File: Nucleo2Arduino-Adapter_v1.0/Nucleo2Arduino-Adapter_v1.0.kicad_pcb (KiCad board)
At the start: 2 copper layers, 68.6 x 53.3 mm, 12 parts, among them J1 TI_BOOSTER_40_J1, J2 TI_BOOSTER_40_J2, J3 TI_BOOSTER_40_J3, J4 TI_BOOSTER_40_J4, P1 Power, P2 Analog, P3 Digital, P4 Digital, P5 CONN_1, P6 CONN_1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

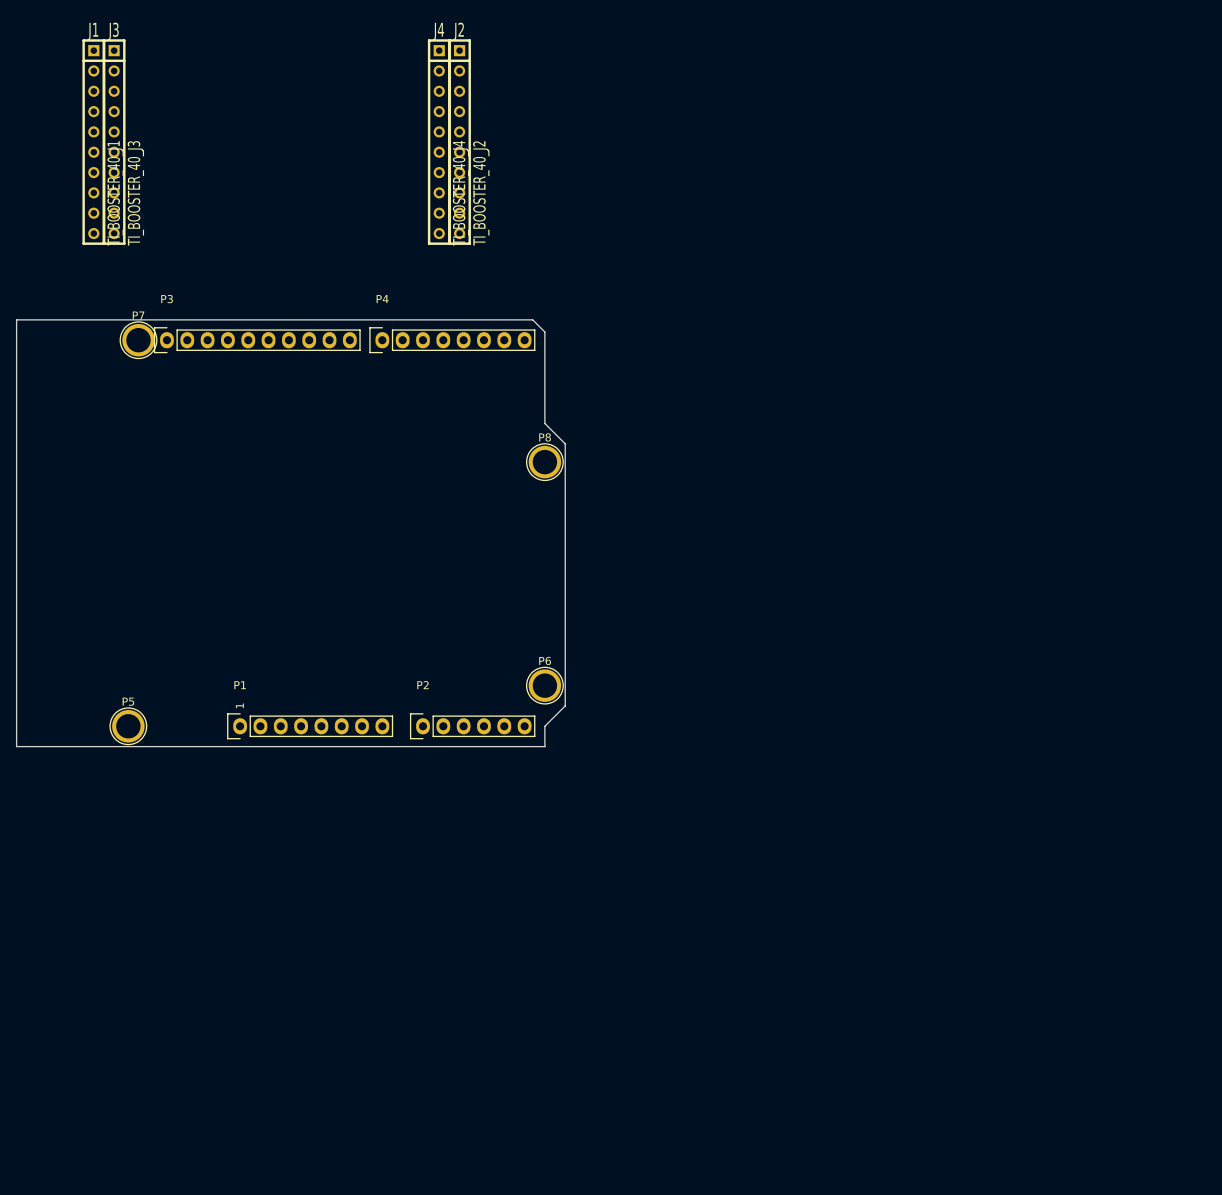
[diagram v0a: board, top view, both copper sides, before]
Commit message: Added ICSP header, Fixed Ardino/BSTPCK Symbols, Added connection
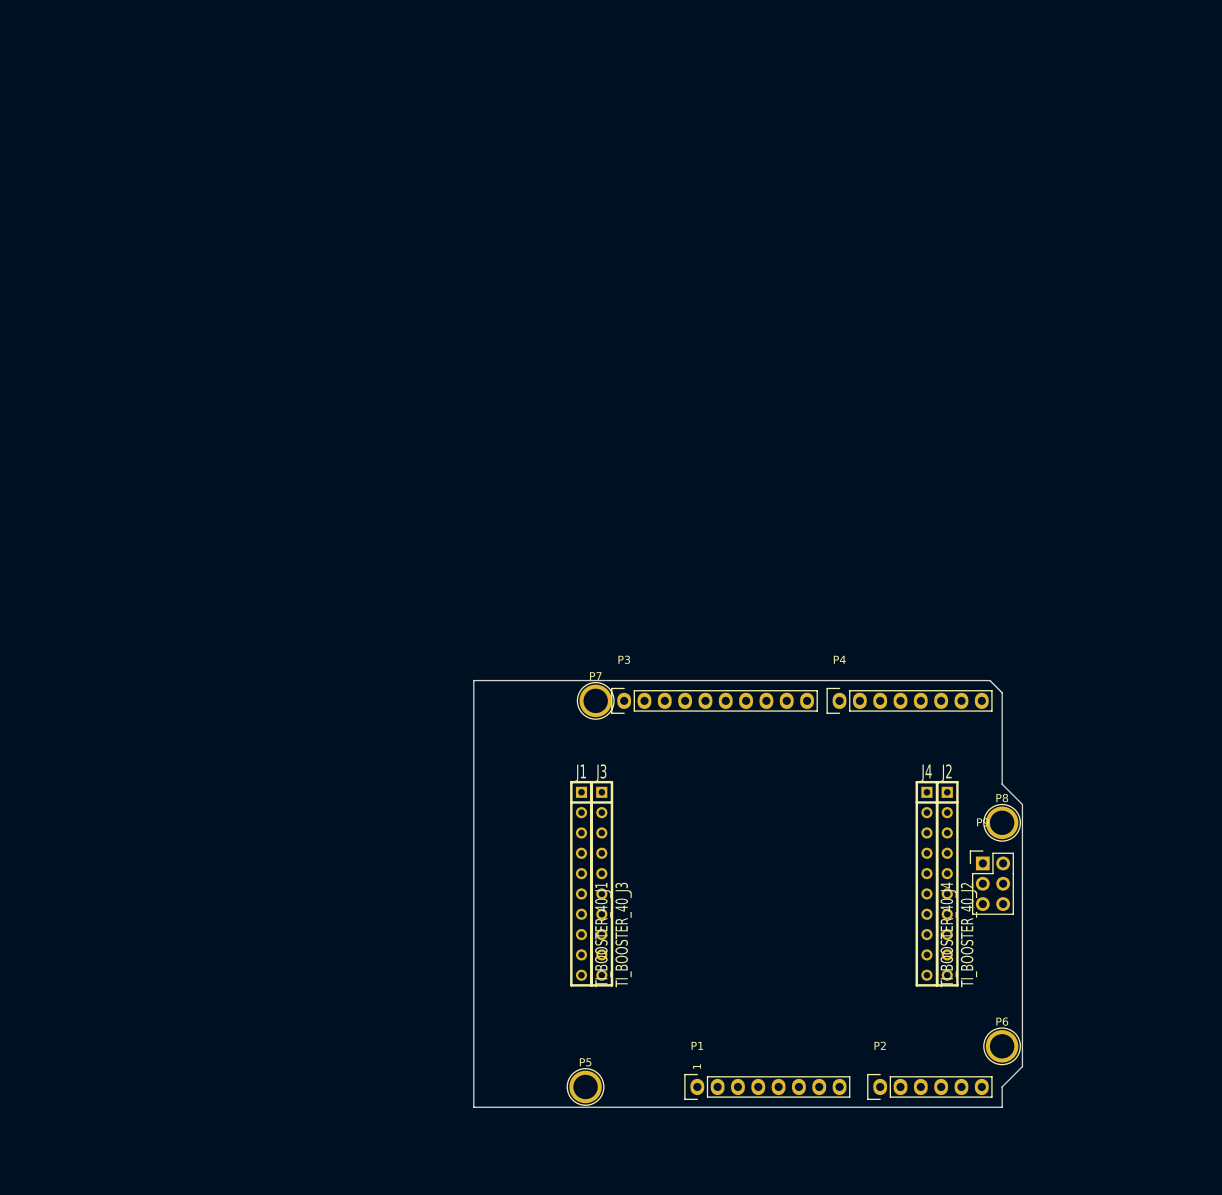
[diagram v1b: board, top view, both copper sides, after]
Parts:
- added P9: ARDUINO_ICSP, Pin_Headers:Pin_Header_Straight_2x03, F.Cu at (244.5, 147.3)
- moved J1 111.0 mm to (194.3, 149.9)
- moved J2 111.0 mm to (240.0, 149.9)
- moved J3 111.0 mm to (196.8, 149.9)
- moved J4 111.0 mm to (237.5, 149.9)
- moved P3 72.8 mm to (199.6, 127.0)
- moved P4 72.8 mm to (226.6, 127.0)
- moved P6 72.8 mm to (246.9, 170.2)
- moved P7 72.8 mm to (196.1, 127.0)
- moved P8 72.8 mm to (246.9, 142.2)
- moved P1 72.8 mm to (208.8, 175.3)
- moved P2 72.8 mm to (231.6, 175.3)
- moved P5 72.8 mm to (194.8, 175.3)
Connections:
- net /10(**/SS) renamed /SPI_0_SS
- net /2 renamed Net-(P4-Pad6)
- net /4 renamed Net-(P4-Pad4)
- net /7 renamed Net-(P4-Pad1)
- net /8 renamed Net-(P3-Pad10)
- net /AREF renamed Net-(P3-Pad3)
- net /IOREF renamed Net-(P1-Pad2)
- net /Vin renamed VDD
- J1 pad 1: VCC -> +3V3
- J1 pad 10: Net-(J1-Pad10) -> /I2C_0_SDA
- J1 pad 2: Net-(J1-Pad2) -> /AIn_0_0
- J1 pad 3: Net-(J1-Pad3) -> /UART_0_RX
- J1 pad 4: Net-(J1-Pad4) -> /UART_0_TX
- J1 pad 6: Net-(J1-Pad6) -> /AIn_0_1
- J1 pad 7: Net-(J1-Pad7) -> /SPI_0_SCK
- J1 pad 9: Net-(J1-Pad9) -> /I2C_0_SCL
- J2 pad 2: Net-(J2-Pad2) -> /PWM_0_1
- J2 pad 5: Net-(J2-Pad5) -> /RESET
- J2 pad 6: Net-(J2-Pad6) -> /SPI_0_MOSI
- J2 pad 7: Net-(J2-Pad7) -> /SPI_0_MISO
- J3 pad 3: Net-(J3-Pad3) -> /AIn_0_2
- J3 pad 4: Net-(J3-Pad4) -> /AIn_0_3
- J3 pad 5: Net-(J3-Pad5) -> /AIn_0_4
- J3 pad 6: Net-(J3-Pad6) -> /AIn_0_5
- J4 pad 1: Net-(J4-Pad1) -> /PWM_0_2
- J4 pad 2: Net-(J4-Pad2) -> /PWM_0_3
- J4 pad 3: Net-(J4-Pad3) -> /PWM_0_4
- P1 pad 3: /Reset -> /RESET
- P2 pad 1: /A0 -> /AIn_0_0
- P2 pad 2: /A1 -> /AIn_0_1
- P2 pad 3: /A2 -> /AIn_0_2
- P2 pad 4: /A3 -> /AIn_0_3
- P2 pad 5: /A4(SDA) -> /AIn_0_4
- P2 pad 6: /A5(SCL) -> /AIn_0_5
- P3 pad 1: /A5(SCL) -> /I2C_0_SCL
- P3 pad 2: /A4(SDA) -> /I2C_0_SDA
- P3 pad 5: /13(SCK) -> /SPI_0_SCK
- P3 pad 6: /12(MISO) -> /SPI_0_MISO
- P3 pad 7: /11(**/MOSI) -> /SPI_0_MOSI
- P3 pad 9: /9(**) -> /PWM_0_1
- P4 pad 2: /6(**) -> /PWM_0_2
- P4 pad 3: /5(**) -> /PWM_0_3
- P4 pad 5: /3(**) -> /PWM_0_4
- P4 pad 7: /1(Tx) -> /UART_0_TX
- P4 pad 8: /0(Rx) -> /UART_0_RX

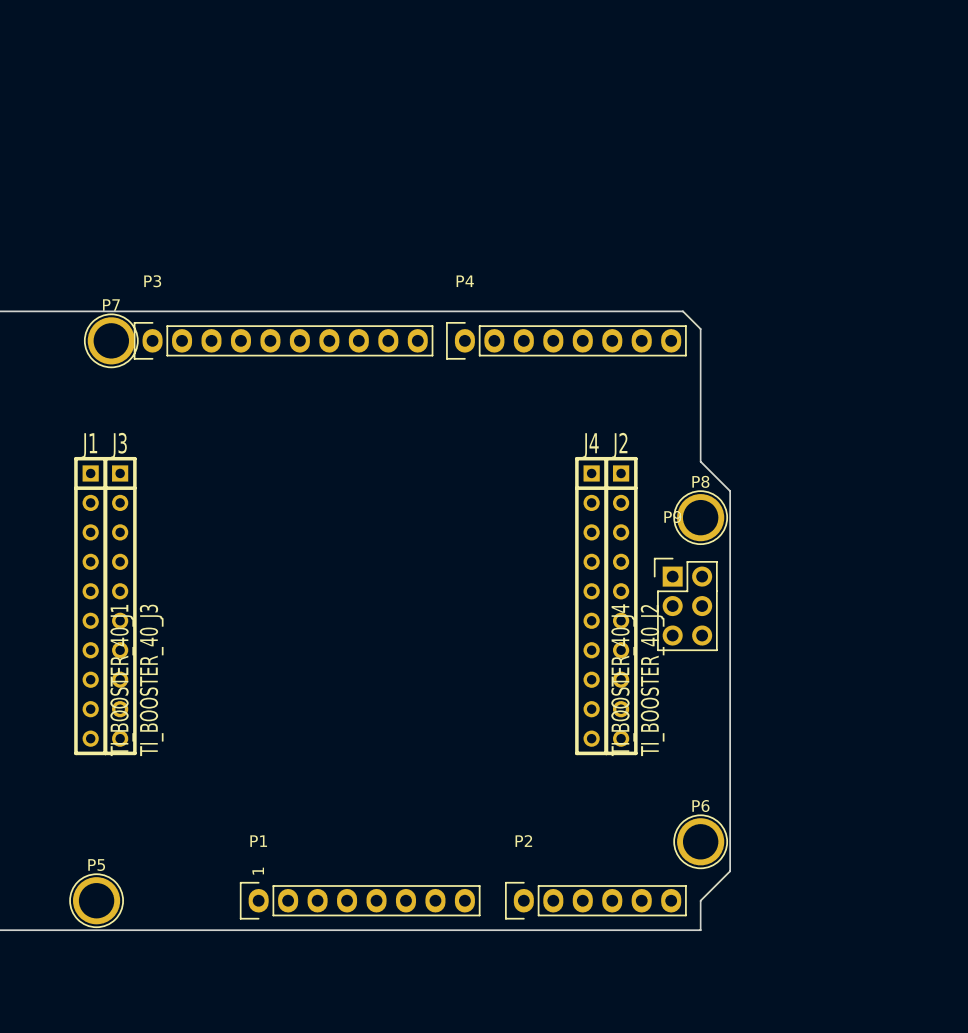
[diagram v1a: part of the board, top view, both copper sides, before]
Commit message: added Nucleo Zio and Atmel XPro Header symbol
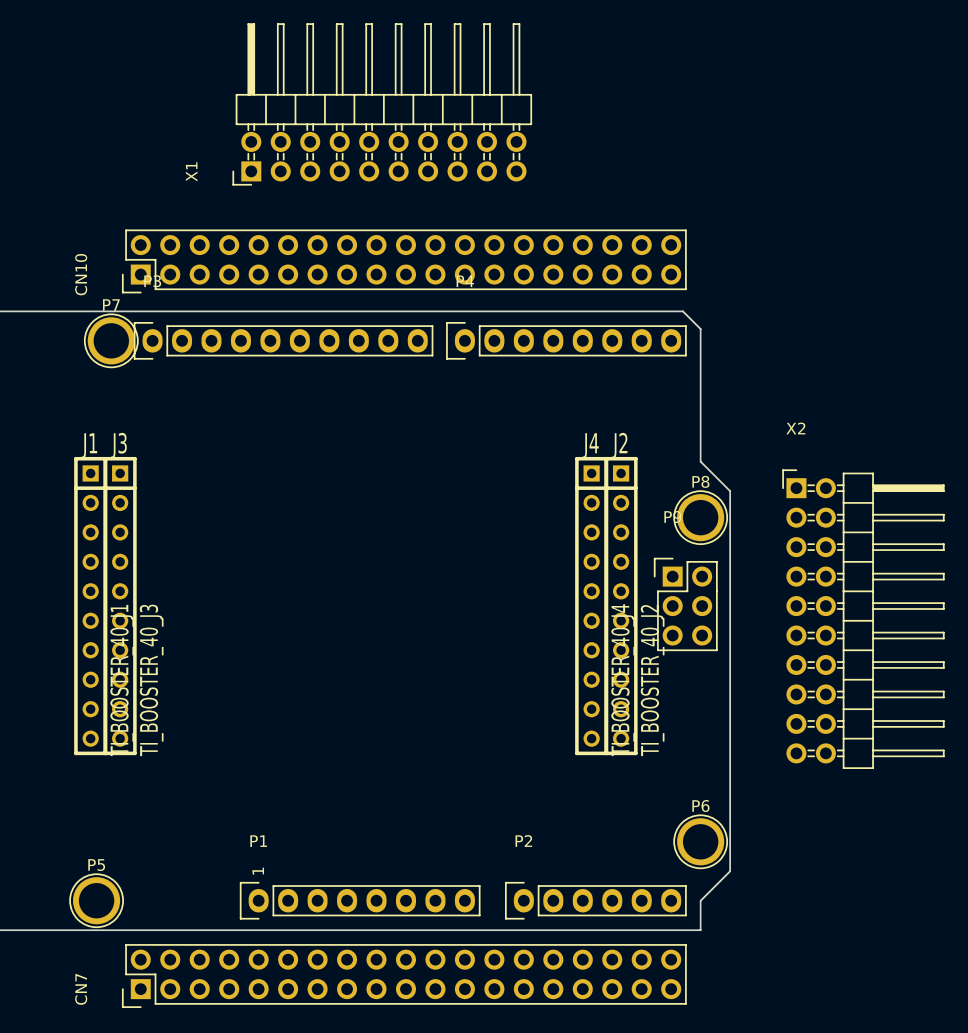
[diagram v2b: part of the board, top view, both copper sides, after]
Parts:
- added CN10: NUCLEO_CN10, Pin_Headers:Pin_Header_Straight_2x19, F.Cu at (198.6, 121.3)
- added CN7: NUCLEO_CN7, Pin_Headers:Pin_Header_Straight_2x19, F.Cu at (198.6, 182.9)
- added X1: Atmel_XPRO_ADDON, Pin_Headers:Pin_Header_Angled_2x10, F.Cu at (208.2, 112.4)
- added X2: Atmel_XPRO_ADDON, Pin_Headers:Pin_Header_Angled_2x10, F.Cu at (255.1, 139.7)
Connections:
- J1 pad 5: Net-(J1-Pad5) -> /INT_0_0
- J1 pad 6: /AIn_0_1 -> /AIn_0_3
- J1 pad 8: Net-(J1-Pad8) -> /INT_0_1
- J2 pad 10: Net-(J2-Pad10) -> /AIn_0_2
- J2 pad 2: /PWM_0_1 -> /PWM_0_5
- J2 pad 3: Net-(J2-Pad3) -> /AIn_0_4
- J2 pad 4: Net-(J2-Pad4) -> /AIn_0_5
- J2 pad 8: Net-(J2-Pad8) -> /SPI_0_SS
- J2 pad 9: Net-(J2-Pad9) -> /AIn_0_1
- J3 pad 10: Net-(J3-Pad10) -> /SPI_1_MISO
- J3 pad 3: /AIn_0_2 -> Net-(J3-Pad3)
- J3 pad 4: /AIn_0_3 -> Net-(J3-Pad4)
- J3 pad 5: /AIn_0_4 -> Net-(J3-Pad5)
- J3 pad 6: /AIn_0_5 -> Net-(J3-Pad6)
- J3 pad 7: Net-(J3-Pad7) -> /SPI_1_SS
- J3 pad 8: Net-(J3-Pad8) -> /SPI_1_SCK
- J3 pad 9: Net-(J3-Pad9) -> /SPI_1_MOSI
- J4 pad 1: /PWM_0_2 -> /PWM_0_1
- J4 pad 2: /PWM_0_3 -> /PWM_0_2
- J4 pad 3: /PWM_0_4 -> /PWM_0_3
- J4 pad 4: Net-(J4-Pad4) -> /PWM_0_4
- P3 pad 10: Net-(P3-Pad10) -> /SPI_1_SS
- P4 pad 1: Net-(P4-Pad1) -> /PWM_0_4
- P4 pad 4: Net-(P4-Pad4) -> /PWM_0_5
- P4 pad 5: /PWM_0_4 -> /INT_0_1
- P4 pad 6: Net-(P4-Pad6) -> /INT_0_0
- P9 pad 1: /SPI_0_MISO -> /SPI_1_MISO
- P9 pad 3: /SPI_0_SCK -> /SPI_1_SCK
- P9 pad 4: /SPI_0_MOSI -> /SPI_1_MOSI

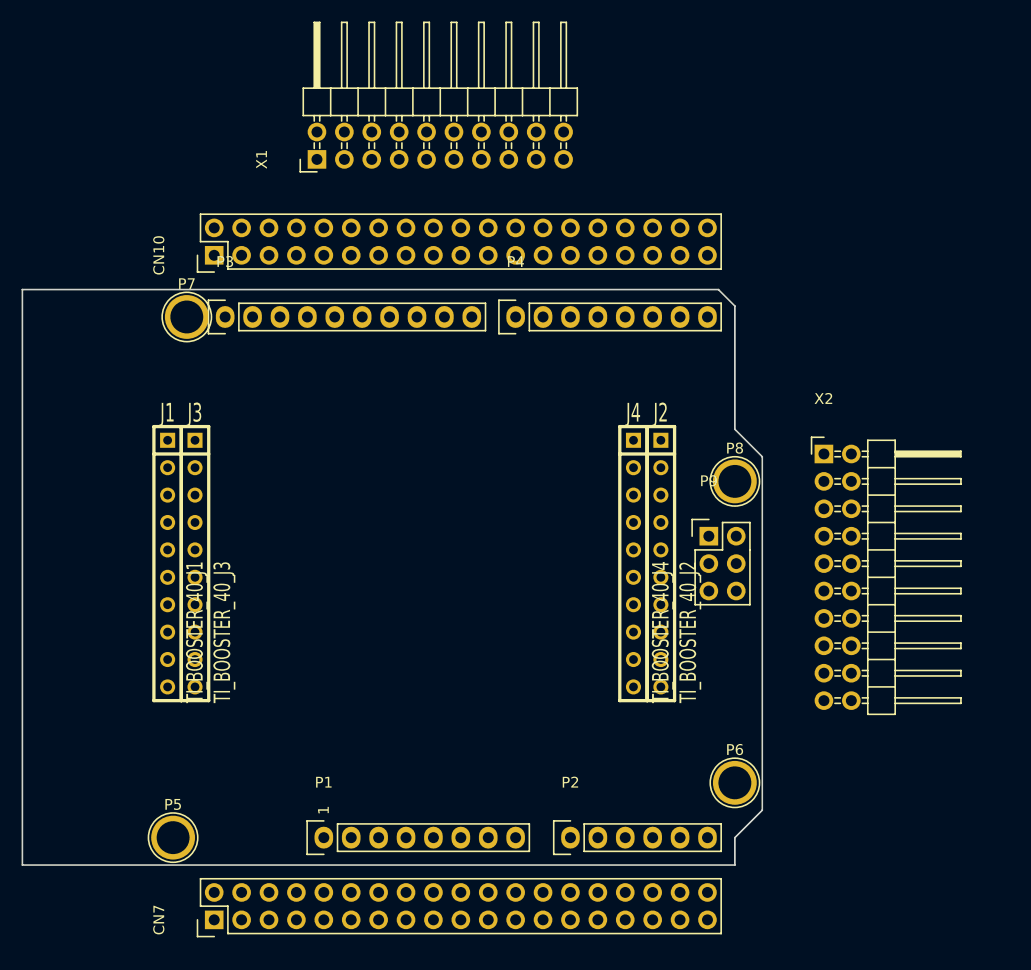
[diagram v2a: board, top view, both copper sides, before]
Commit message: First draft of connection. Completed PCB pin position
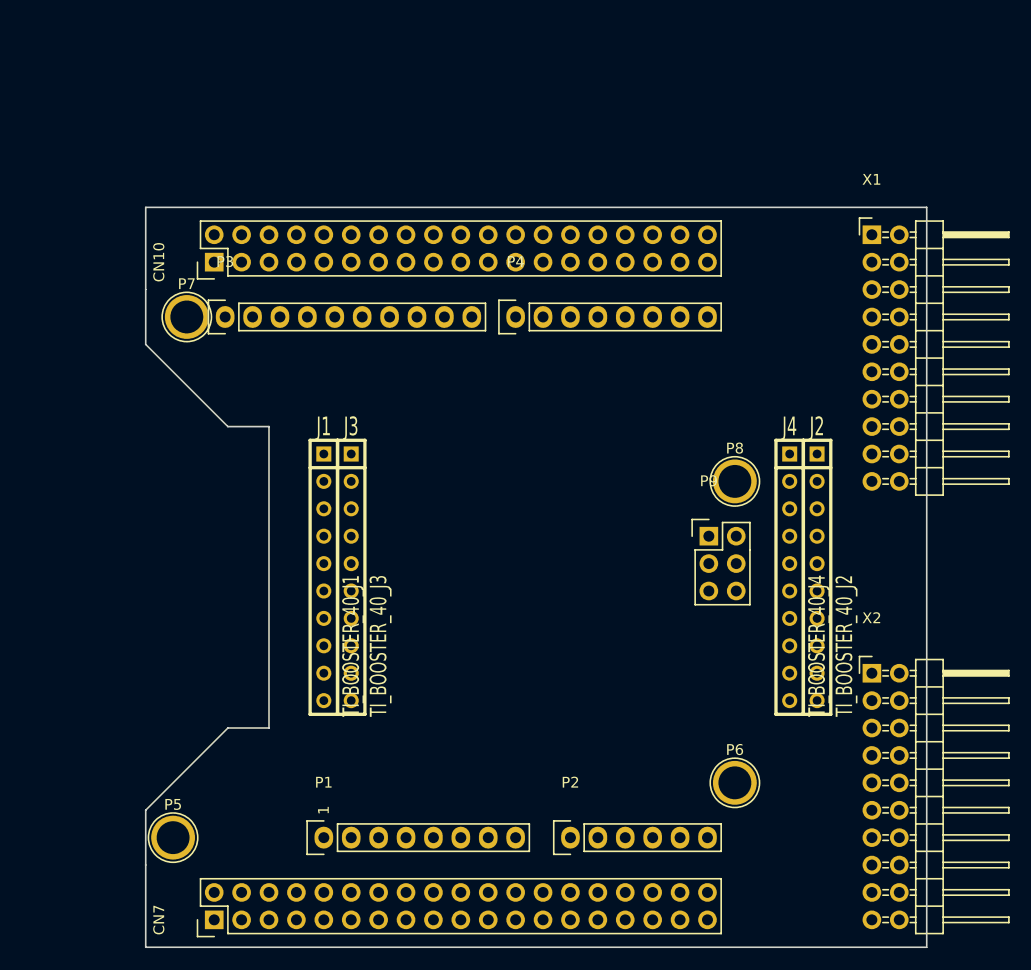
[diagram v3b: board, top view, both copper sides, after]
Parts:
- moved X1 51.9 mm to (259.6, 119.4), turned to 0 degrees
- moved X2 20.8 mm to (259.6, 160.0)
- moved J1 14.5 mm to (208.8, 151.1)
- moved J2 14.5 mm to (254.5, 151.1)
- moved J3 14.5 mm to (211.3, 151.1)
- moved J4 14.5 mm to (252.0, 151.1)
- moved CN10 0.64 mm to (198.6, 121.9)
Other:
- board size 68.6 x 53.3 mm -> 72.4 x 68.6 mm
